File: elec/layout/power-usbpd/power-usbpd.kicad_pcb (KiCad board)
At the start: 2 copper layers, 0 parts

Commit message: update syntax for signal to line, basic placement
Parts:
- added C1: 4.7µF ±10% 35V X5R, atopile:C0603-bd72f6, F.Cu at (84.6, 72.8)
- added C2: 1µF ±10% 25V X5R, atopile:C0402-b3ef17, F.Cu at (92.6, 77.0)
- added C3: 1µF ±10% 25V X5R, atopile:C0402-b3ef17, F.Cu at (93.6, 77.0)
- added C4: 100nF ±10% 16V X7R, atopile:C0402-b3ef17, F.Cu at (88.1, 71.8)
- added D1: , atopile:SOT-323-3_L2.1-W1.3-P1.32-LS2.1-BR-ee9edb, F.Cu at (85.8, 75.4)
- added D2: , atopile:DFN1610-2_L1.6-W1.0-P1.05-RD-57a24e, F.Cu at (84.6, 70.3)
- added D3: , atopile:DFN1610-2_L1.6-W1.0-P1.05-RD-57a24e, F.Cu at (84.6, 67.9)
- added Q1: , atopile:PDFN3333-8_L3.1-W3.2-P0.65-LS3.4-BL-33e04e, F.Cu at (87.2, 68.5)
- added R1: 1kΩ ±1% 62.5mW, atopile:R0402-56259e, F.Cu at (86.0, 71.7)
- added R2: 4.7kΩ ±1% 62.5mW, atopile:R0402-56259e, F.Cu at (94.4, 69.5)
- added R3: 4.7kΩ ±1% 62.5mW, atopile:R0402-56259e, F.Cu at (93.4, 69.5)
- added R4: 1kΩ ±1% 62.5mW, atopile:R0402-56259e, F.Cu at (87.1, 71.7)
- added R5: 100kΩ ±1% 62.5mW, atopile:R0402-56259e, F.Cu at (89.4, 68.7)
- added R6: 22kΩ ±1% 62.5mW, atopile:R0402-56259e, F.Cu at (90.4, 68.7)
- added R7: 100Ω ±1% 62.5mW, atopile:R0402-56259e, F.Cu at (89.4, 70.6)
- added U1: , atopile:QFN-24_L4.0-W4.0-P0.50-BL-EP2.8-2a85a7, F.Cu at (92.6, 73.1)
- added U2: 10kΩ ±1% 62.5mW, atopile:R0402-56259e, F.Cu at (89.5, 80.0)
- added U3: 10kΩ ±1% 62.5mW, atopile:R0402-56259e, F.Cu at (89.5, 79.0)
- added USB1: , atopile:USB-C-SMD_TYC-324G-a50b79, F.Cu at (80.5, 71.5)

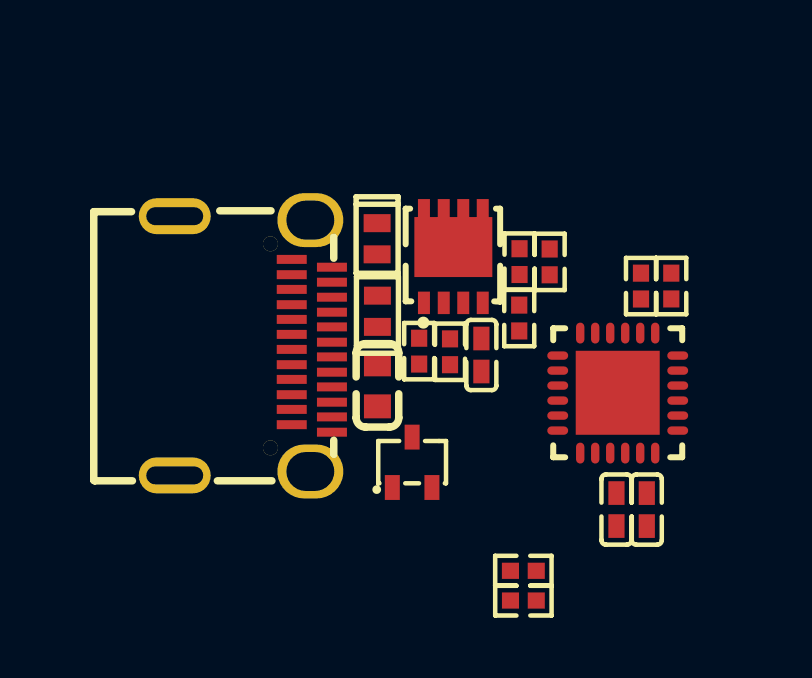
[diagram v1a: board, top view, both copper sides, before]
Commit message: Layout complete for USB PD block
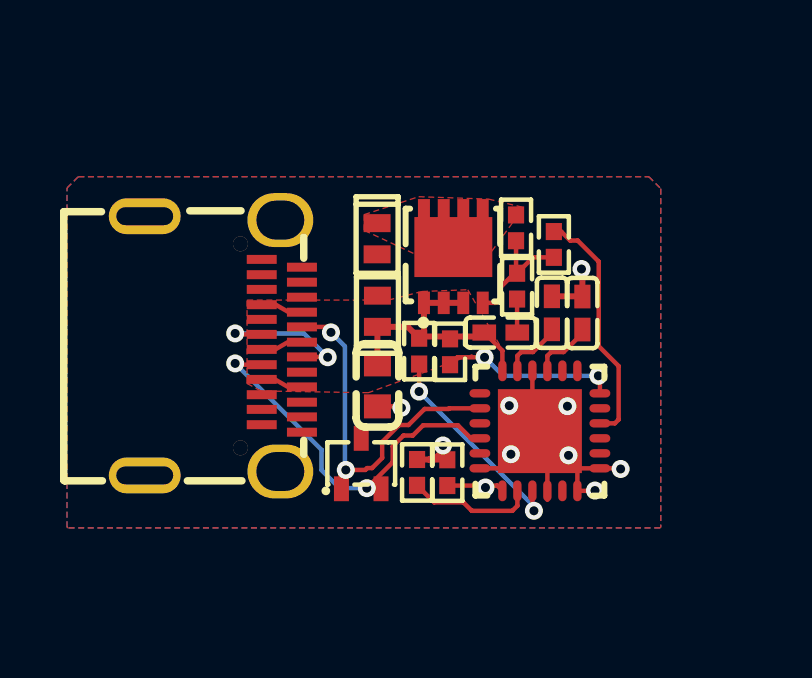
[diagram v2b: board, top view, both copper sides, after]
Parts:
- removed U2, U3: 10kΩ ±1% 62.5mW, atopile:R0402-56259e
- moved R2 9.72 mm to (87.0, 75.7)
- moved R3 9.71 mm to (86.0, 75.7)
- moved C3 7.28 mm to (90.5, 70.4), turned to -90 degrees
- moved C2 6.65 mm to (91.5, 70.4), turned to -90 degrees
- moved U1 2.88 mm to (90.1, 74.3), turned to -90 degrees
- moved D1 1.70 mm to (84.1, 75.4)
- moved R5 1.13 mm to (89.3, 67.6)
- moved R7 1.06 mm to (89.3, 69.5)
- moved USB1 1.00 mm to (79.5, 71.5)
- moved C4 0.99 mm to (88.7, 71.1), turned to 180 degrees
- moved R6 0.60 mm to (90.5, 68.1)
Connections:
- net SBU2 renamed B8
- net SSRXN2 renamed A10
- net SSRXP2 renamed A11
- net SSTXN2 renamed B3
- net SSTXP2 renamed B2
- net pd_controller-line renamed line
- net pd_controller-line-1 renamed line-1
- U1 pad 1: pd_controller.pd_controller-line -> pd_controller.pd_controller-line-1
- U1 pad 5: pd_controller.pd_controller-line-1 -> pd_controller.pd_controller-line
- USB1 pad 1: usb_connector.footprint.pins[0].net-net -> gnd
- USB1 pad 2: usb_connector.footprint.pins[1].net-net -> gnd
- USB1 pad 3: usb_connector.footprint.pins[2].net-net -> gnd
- USB1 pad 4: usb_connector.footprint.pins[3].net-net -> gnd
- USB1 pad A5: (no net) -> CC1
- USB1 pad B5: (no net) -> CC2
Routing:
- net gnd: track 0.00 -> 16.1 mm, vias 0 -> 8
- net CC2: track 0.00 -> 12.5 mm, vias 0 -> 2
- net CC1: track 0.00 -> 12.4 mm, vias 0 -> 2
- net VBUS: track 0.00 -> 9.89 mm
- net VBUS_EN_SNK: track 0.00 -> 8.13 mm
- net DISCH: track 0.00 -> 7.17 mm, vias 0 -> 2
- net VBUS_VS_DISCH: track 0.00 -> 5.91 mm, vias 0 -> 2
- net dm: track 0.00 -> 5.17 mm, vias 0 -> 2
- net gate: track 0.00 -> 4.31 mm
- net line-1: track 0.00 -> 4.26 mm
- net line: track 0.00 -> 2.17 mm, vias 0 -> 1
- net VREG_1V2: track 0.00 -> 2.10 mm
- net VREG_2V7: track 0.00 -> 2.09 mm
- net hv: track 0.00 -> 1.77 mm, vias 0 -> 1
- net pd_controller-net: track 0.00 -> 1.12 mm
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- added copper zone on F.Cu, net VBUS
- added copper zone on F.Cu, net VSINK_VCC
- added copper zone on B.Cu, net gnd
- added copper zone on F.Cu, net gnd

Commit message: remove default build, build everything locally
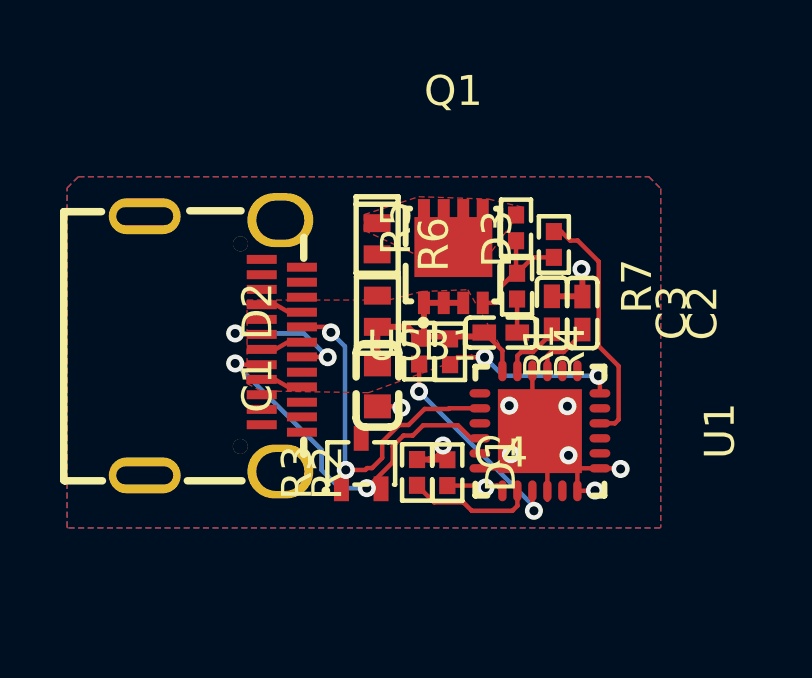
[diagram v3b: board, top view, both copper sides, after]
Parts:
- USB1: footprint atopile:USB-C-SMD_TYC-324G-a50b79 -> lib:USB-C-SMD_TYC-324G-a50b79

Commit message: add module builds back in to ato.yaml with mfg-data excluded in config
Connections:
- net A8 renamed SBU1
- net B10 renamed SSRXN1
- net B11 renamed SSRXP1
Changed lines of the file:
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@@
     (net 12 "gnd")
     (net 13 "dp")
-    (net 14 "B10")
+    (net 14 "SSRXN1")
     (net 15 "GPIO")
     (net 16 "POWER_OK3")
-    (net 17 "B11")
+    (net 17 "SSRXP1")
     (net 18 "VREG_2V7")
     (net 19 "A_B_SIDE")
@@
     (net 28 "VSINK_VCC")
     (net 29 "B8")
-    (net 30 "A8")
+    (net 30 "SBU1")
     (net 31 "A11")
     (net 32 "CC2")
@@
             (layers "F.Cu" "F.Paste" "F.Mask")
             (remove_unused_layers no)
-            (net 30 "A8"))
+            (net 30 "SBU1"))
         (pad "A9" smd rect
             (at 1.37 -2.62 -90)
@@
             (layers "F.Cu" "F.Paste" "F.Mask")
             (remove_unused_layers no)
-            (net 14 "B10"))
+            (net 14 "SSRXN1"))
         (pad "B11" smd rect
             (at -2.37 -1.28 -90)
@@
             (layers "F.Cu" "F.Paste" "F.Mask")
             (remove_unused_layers no)
-            (net 17 "B11"))
+            (net 17 "SSRXP1"))
         (pad "B12" smd rect
             (at -2.88 -1.28 -90)

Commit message: add CAN isolator, cellsim cell
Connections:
- net SBU1 renamed A8
- net SSRXN1 renamed B10
- net SSRXP1 renamed B11
- R2 pad 1: line -> line-1
- R3 pad 1: line-1 -> line
- U1 pad 7: line -> line-1
- U1 pad 8: line-1 -> line
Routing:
- net line-1: track 4.26 -> 2.17 mm, vias 0 -> 1
- net line: track 2.17 -> 4.26 mm, vias 1 -> 0
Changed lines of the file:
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@@
     (net 12 "gnd")
     (net 13 "dp")
-    (net 14 "SSRXN1")
+    (net 14 "B10")
     (net 15 "GPIO")
     (net 16 "POWER_OK3")
-    (net 17 "SSRXP1")
+    (net 17 "B11")
     (net 18 "VREG_2V7")
     (net 19 "A_B_SIDE")
@@
     (net 28 "VSINK_VCC")
     (net 29 "B8")
-    (net 30 "SBU1")
+    (net 30 "A8")
     (net 31 "A11")
     (net 32 "CC2")
-    (net 33 "line-1")
+    (net 33 "line")
     (net 34 "CC1")
     (net 35 "hv")
-    (net 36 "line")
+    (net 36 "line-1")
     (footprint "atopile:QFN-24_L4.0-W4.0-P0.50-BL-EP2.8-2a85a7"
         (layer "F.Cu")
@@
             (layers "F.Cu" "F.Paste" "F.Mask")
             (remove_unused_layers no)
-            (net 36 "line"))
+            (net 36 "line-1"))
         (pad "8" smd oval
             (at 2 0.75 0)
@@
             (layers "F.Cu" "F.Paste" "F.Mask")
             (remove_unused_layers no)
-            (net 33 "line-1"))
+            (net 33 "line"))
         (pad "9" smd oval
             (at 2 0.25 0)
@@
             (layers "F.Cu" "F.Paste" "F.Mask")
             (remove_unused_layers no)
-            (net 30 "SBU1"))
+            (net 30 "A8"))
         (pad "A9" smd rect
             (at 1.37 -2.62 -90)
@@
             (layers "F.Cu" "F.Paste" "F.Mask")
             (remove_unused_layers no)
-            (net 14 "SSRXN1"))
+            (net 14 "B10"))
         (pad "B11" smd rect
             (at -2.37 -1.28 -90)
@@
             (layers "F.Cu" "F.Paste" "F.Mask")
             (remove_unused_layers no)
-            (net 17 "SSRXP1"))
+            (net 17 "B11"))
         (pad "B12" smd rect
             (at -2.88 -1.28 -90)
@@
             (layers "F.Cu" "F.Paste" "F.Mask")
             (remove_unused_layers no)
-            (net 36 "line"))
+            (net 36 "line-1"))
         (pad "2" smd rect
             (at 0.43 0 90)
@@
             (layers "F.Cu" "F.Paste" "F.Mask")
             (remove_unused_layers no)
-            (net 33 "line-1"))
+            (net 33 "line"))
         (pad "2" smd rect
             (at 0.43 0 90)

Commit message: rebuild all modules
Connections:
- net A2 renamed SSTXP1
- net A3 renamed SSTXN1
- net A8 renamed SBU1
- net B10 renamed SSRXN1
- net B11 renamed SSRXP1
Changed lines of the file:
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@@
     (net 1 "B3")
     (net 2 "A10")
-    (net 3 "A3")
+    (net 3 "SSTXN1")
     (net 4 "VBUS")
     (net 5 "pd_controller.pd_controller-line-1")
@@
     (net 12 "gnd")
     (net 13 "dp")
-    (net 14 "B10")
+    (net 14 "SSRXN1")
     (net 15 "GPIO")
     (net 16 "POWER_OK3")
-    (net 17 "B11")
+    (net 17 "SSRXP1")
     (net 18 "VREG_2V7")
     (net 19 "A_B_SIDE")
@@
     (net 21 "dm")
     (net 22 "pd_controller-net")
-    (net 23 "A2")
+    (net 23 "SSTXP1")
     (net 24 "POWER_OK2")
     (net 25 "pd_controller.pd_controller-line")
@@
     (net 28 "VSINK_VCC")
     (net 29 "B8")
-    (net 30 "A8")
+    (net 30 "SBU1")
     (net 31 "A11")
     (net 32 "CC2")
@@
             (layers "F.Cu" "F.Paste" "F.Mask")
             (remove_unused_layers no)
-            (net 23 "A2"))
+            (net 23 "SSTXP1"))
         (pad "A3" smd rect
             (at -1.62 -2.62 -90)
@@
             (layers "F.Cu" "F.Paste" "F.Mask")
             (remove_unused_layers no)
-            (net 3 "A3"))
+            (net 3 "SSTXN1"))
         (pad "A4" smd rect
             (at -1.12 -2.62 -90)
@@
             (layers "F.Cu" "F.Paste" "F.Mask")
             (remove_unused_layers no)
-            (net 30 "A8"))
+            (net 30 "SBU1"))
         (pad "A9" smd rect
             (at 1.37 -2.62 -90)
@@
             (layers "F.Cu" "F.Paste" "F.Mask")
             (remove_unused_layers no)
-            (net 14 "B10"))
+            (net 14 "SSRXN1"))
         (pad "B11" smd rect
             (at -2.37 -1.28 -90)
@@
             (layers "F.Cu" "F.Paste" "F.Mask")
             (remove_unused_layers no)
-            (net 17 "B11"))
+            (net 17 "SSRXP1"))
         (pad "B12" smd rect
             (at -2.88 -1.28 -90)

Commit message: core layout, rebuild modules with compiler updates
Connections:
- net SBU1 renamed A8
- U1 pad 1: pd_controller.pd_controller-line-1 -> pd_controller.pd_controller-line
- U1 pad 5: pd_controller.pd_controller-line -> pd_controller.pd_controller-line-1
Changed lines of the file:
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@@
     (net 3 "SSTXN1")
     (net 4 "VBUS")
-    (net 5 "pd_controller.pd_controller-line-1")
+    (net 5 "pd_controller.pd_controller-line")
     (net 6 "ATTACH")
     (net 7 "pd_controller.pd_controller.footprint.pins[18].net-net")
@@
     (net 23 "SSTXP1")
     (net 24 "POWER_OK2")
-    (net 25 "pd_controller.pd_controller-line")
+    (net 25 "pd_controller.pd_controller-line-1")
     (net 26 "B2")
     (net 27 "VBUS_VS_DISCH")
     (net 28 "VSINK_VCC")
     (net 29 "B8")
-    (net 30 "SBU1")
+    (net 30 "A8")
     (net 31 "A11")
     (net 32 "CC2")
@@
             (layers "F.Cu" "F.Paste" "F.Mask")
             (remove_unused_layers no)
-            (net 5 "pd_controller.pd_controller-line-1"))
+            (net 5 "pd_controller.pd_controller-line"))
         (pad "2" smd oval
             (at -0.75 2 90)
@@
             (layers "F.Cu" "F.Paste" "F.Mask")
             (remove_unused_layers no)
-            (net 25 "pd_controller.pd_controller-line"))
+            (net 25 "pd_controller.pd_controller-line-1"))
         (pad "6" smd oval
             (at 1.25 2 90)
@@
             (layers "F.Cu" "F.Paste" "F.Mask")
             (remove_unused_layers no)
-            (net 30 "SBU1"))
+            (net 30 "A8"))
         (pad "A9" smd rect
             (at 1.37 -2.62 -90)

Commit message: Everything builds
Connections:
- net B8 renamed SBU2
- net SSRXN1 renamed B10
- net SSRXP1 renamed B11
- net SSTXN1 renamed A3
- net SSTXP1 renamed A2
- net dp renamed line-3
- R2 pad 1: line-1 -> line-2
- U1 pad 1: pd_controller.pd_controller-line -> pd_controller.pd_controller-line-1
- U1 pad 5: pd_controller.pd_controller-line-1 -> pd_controller.pd_controller-line
- U1 pad 7: line-1 -> line-2
- USB1 pad A7: dm -> line-1
- USB1 pad B7: dm -> line-1
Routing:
- net dm: track 5.17 -> 0.00 mm, vias 2 -> 0
- net line-1: track 2.17 -> 5.17 mm, vias 1 -> 2
- net line-2: track 0.00 -> 2.17 mm, vias 0 -> 1
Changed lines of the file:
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@@
     (net 1 "B3")
     (net 2 "A10")
-    (net 3 "SSTXN1")
+    (net 3 "A3")
     (net 4 "VBUS")
-    (net 5 "pd_controller.pd_controller-line")
+    (net 5 "pd_controller.pd_controller-line-1")
     (net 6 "ATTACH")
     (net 7 "pd_controller.pd_controller.footprint.pins[18].net-net")
@@
     (net 11 "VBUS_EN_SNK")
     (net 12 "gnd")
-    (net 13 "dp")
-    (net 14 "SSRXN1")
+    (net 13 "line-3")
+    (net 14 "B10")
     (net 15 "GPIO")
     (net 16 "POWER_OK3")
-    (net 17 "SSRXP1")
+    (net 17 "B11")
     (net 18 "VREG_2V7")
     (net 19 "A_B_SIDE")
     (net 20 "DISCH")
-    (net 21 "dm")
+    (net 21 "line-1")
     (net 22 "pd_controller-net")
-    (net 23 "SSTXP1")
+    (net 23 "A2")
     (net 24 "POWER_OK2")
-    (net 25 "pd_controller.pd_controller-line-1")
+    (net 25 "pd_controller.pd_controller-line")
     (net 26 "B2")
     (net 27 "VBUS_VS_DISCH")
     (net 28 "VSINK_VCC")
-    (net 29 "B8")
+    (net 29 "SBU2")
     (net 30 "A8")
     (net 31 "A11")
@@
     (net 34 "CC1")
     (net 35 "hv")
-    (net 36 "line-1")
+    (net 36 "line-2")
     (footprint "atopile:QFN-24_L4.0-W4.0-P0.50-BL-EP2.8-2a85a7"
         (layer "F.Cu")
@@
             (layers "F.Cu" "F.Paste" "F.Mask")
             (remove_unused_layers no)
-            (net 5 "pd_controller.pd_controller-line"))
+            (net 5 "pd_controller.pd_controller-line-1"))
         (pad "2" smd oval
             (at -0.75 2 90)
@@
             (layers "F.Cu" "F.Paste" "F.Mask")
             (remove_unused_layers no)
-            (net 25 "pd_controller.pd_controller-line-1"))
+            (net 25 "pd_controller.pd_controller-line"))
         (pad "6" smd oval
             (at 1.25 2 90)
@@
             (layers "F.Cu" "F.Paste" "F.Mask")
             (remove_unused_layers no)
-            (net 36 "line-1"))
+            (net 36 "line-2"))
         (pad "8" smd oval
             (at 2 0.75 0)
@@
             (layers "F.Cu" "F.Paste" "F.Mask")
             (remove_unused_layers no)
-            (net 23 "SSTXP1"))
+            (net 23 "A2"))
         (pad "A3" smd rect
             (at -1.62 -2.62 -90)
@@
             (layers "F.Cu" "F.Paste" "F.Mask")
             (remove_unused_layers no)
-            (net 3 "SSTXN1"))
+            (net 3 "A3"))
         (pad "A4" smd rect
             (at -1.12 -2.62 -90)
@@
             (layers "F.Cu" "F.Paste" "F.Mask")
             (remove_unused_layers no)
-            (net 13 "dp"))
+            (net 13 "line-3"))
         (pad "A7" smd rect
             (at 0.37 -2.62 -90)
@@
             (layers "F.Cu" "F.Paste" "F.Mask")
             (remove_unused_layers no)
-            (net 21 "dm"))
+            (net 21 "line-1"))
         (pad "A8" smd rect
             (at 0.88 -2.62 -90)
@@
             (layers "F.Cu" "F.Paste" "F.Mask")
             (remove_unused_layers no)
-            (net 13 "dp"))
+            (net 13 "line-3"))
         (pad "B7" smd rect
             (at -0.38 -1.28 -90)
@@
             (layers "F.Cu" "F.Paste" "F.Mask")
             (remove_unused_layers no)
-            (net 21 "dm"))
+            (net 21 "line-1"))
         (pad "B8" smd rect
             (at -0.88 -1.28 -90)
@@
             (layers "F.Cu" "F.Paste" "F.Mask")
             (remove_unused_layers no)
-            (net 29 "B8"))
+            (net 29 "SBU2"))
         (pad "B9" smd rect
             (at -1.37 -1.28 -90)
@@
             (layers "F.Cu" "F.Paste" "F.Mask")
             (remove_unused_layers no)
-            (net 14 "SSRXN1"))
+            (net 14 "B10"))
         (pad "B11" smd rect
             (at -2.37 -1.28 -90)
@@
             (layers "F.Cu" "F.Paste" "F.Mask")
             (remove_unused_layers no)
-            (net 17 "SSRXP1"))
+            (net 17 "B11"))
         (pad "B12" smd rect
             (at -2.88 -1.28 -90)
@@
             (layers "F.Cu" "F.Paste" "F.Mask")
             (remove_unused_layers no)
-            (net 36 "line-1"))
+            (net 36 "line-2"))
         (pad "2" smd rect
             (at 0.43 0 90)
